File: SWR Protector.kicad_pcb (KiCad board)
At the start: 2 copper layers, 100 x 100 mm, 27 parts, among them J1 Barrel_Jack, J2 Barrel_Jack, J3 transceiver, J4 antenna, K2 ATX209, Q1 2N3904, T1 1:12, T2 1:12, U1 LM78L05_TO92, U2 LM358

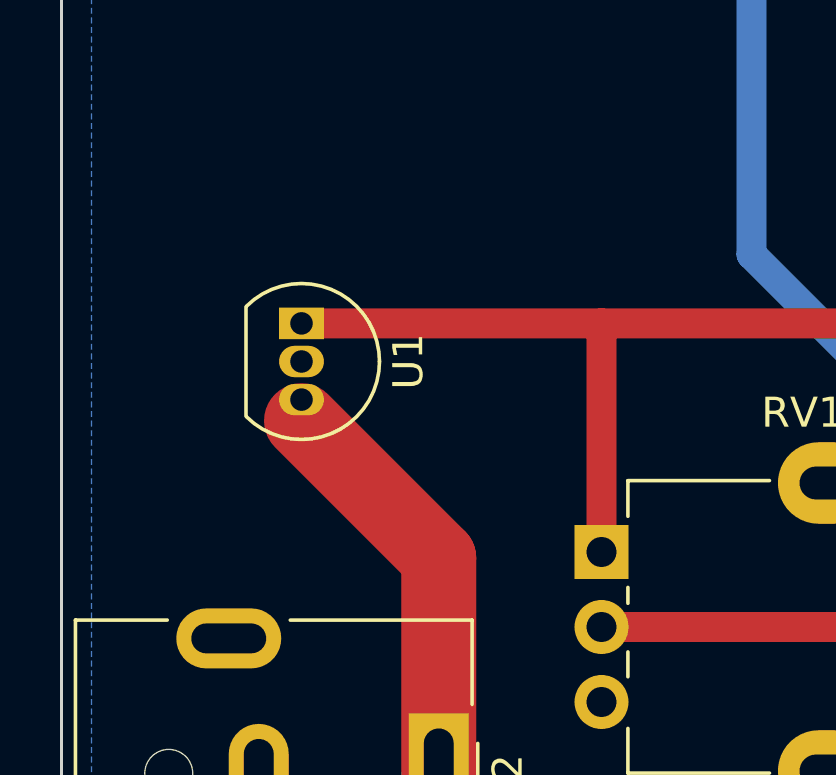
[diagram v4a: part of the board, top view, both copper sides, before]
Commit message: Added a couple of caps on the 5V regulator.
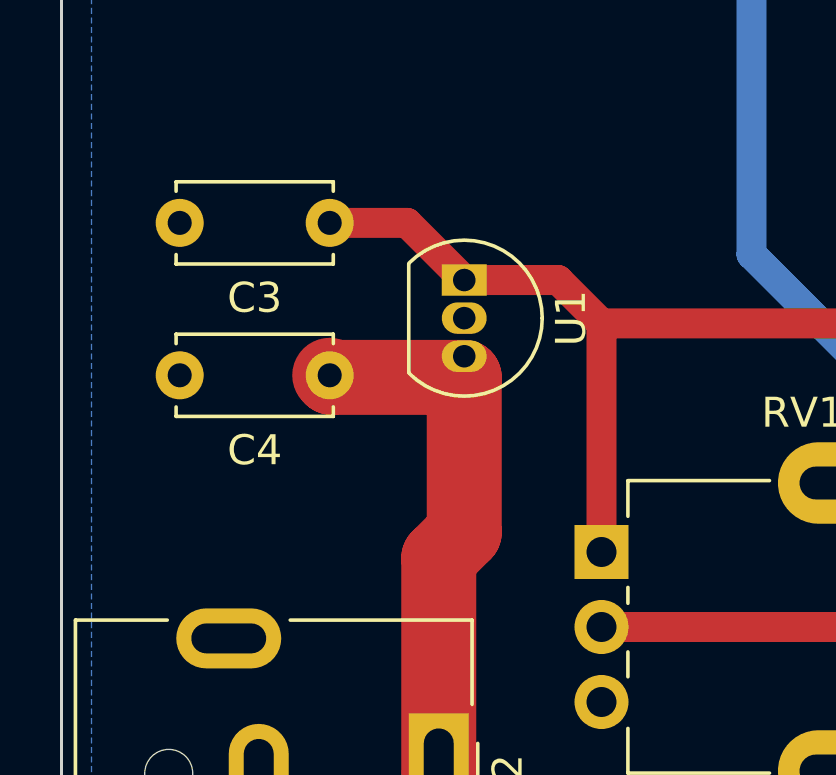
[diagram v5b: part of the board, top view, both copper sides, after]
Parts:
- added C3: 100 nF, Capacitor_THT:C_Disc_D5.0mm_W2.5mm_P5.00mm, F.Cu at (93.9, 120.7)
- added C4: 100 nF, Capacitor_THT:C_Disc_D5.0mm_W2.5mm_P5.00mm, F.Cu at (93.9, 125.7)
- moved U1 5.61 mm to (98.4, 122.6)
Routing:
- net +12V: track 82.4 -> 86.8 mm
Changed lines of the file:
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@@
   )
   (footprint "Package_TO_SOT_THT:TO-92_Inline" (layer "F.Cu")
-    (at 93 124 -90)
+    (at 98.425 122.555 -90)
     (descr "TO-92 leads in-line, narrow, oval pads, drill 0.75mm (see NXP sot054_po.pdf)")
     (tags "to-92 sc-43 sc-43a sot54 PA33 transistor")
@@
     )
   )
+  (footprint "Capacitor_THT:C_Disc_D5.0mm_W2.5mm_P5.00mm" (layer "F.Cu")
+    (at 93.94 120.65 180)
+    (descr "C, Disc series, Radial, pin pitch=5.00mm, , diameter*width=5*2.5mm^2, Capacitor, http://cdn-reichelt.de/documents/datenblatt/B300/DS_KERKO_TC.pdf")
+    (tags "C Disc series Radial pin pitch 5.00mm  diameter 5mm width 2.5mm Capacitor")
+    (property "Sheetfile" "SWR Protector.kicad_sch")
+    (property "Sheetname" "")
+    (property "ki_description" "Unpolarized capacitor")
+    (property "ki_keywords" "cap capacitor")
+    (attr through_hole)
+    (fp_text reference "C3" (at 2.5 -2.5) (layer "F.SilkS")
+        (effects (font (size 1 1) (thickness 0.15)))
+    )
+    (fp_text value "100 nF" (at 2.5 2.5) (layer "F.Fab")
+        (effects (font (size 1 1) (thickness 0.15)))
+    )
+    (fp_text user "${REFERENCE}" (at 2.5 0) (layer "F.Fab")
+        (effects (font (size 1 1) (thickness 0.15)))
+    )
+    (fp_line (start -0.12 -1.37) (end -0.12 -1.055)
+      (stroke (width 0.12) (type solid)) (layer "F.SilkS"))
+    (fp_line (start -0.12 -1.37) (end 5.12 -1.37)
+      (stroke (width 0.12) (type solid)) (layer "F.SilkS"))
+    (fp_line (start -0.12 1.055) (end -0.12 1.37)
+      (stroke (width 0.12) (type solid)) (layer "F.SilkS"))
+    (fp_line (start -0.12 1.37) (end 5.12 1.37)
+      (stroke (width 0.12) (type solid)) (layer "F.SilkS"))
+    (fp_line (start 5.12 -1.37) (end 5.12 -1.055)
+      (stroke (width 0.12) (type solid)) (layer "F.SilkS"))
+    (fp_line (start 5.12 1.055) (end 5.12 1.37)
+      (stroke (width 0.12) (type solid)) (layer "F.SilkS"))
+    (fp_line (start -1.05 -1.5) (end -1.05 1.5)
+      (stroke (width 0.05) (type solid)) (layer "F.CrtYd"))
+    (fp_line (start -1.05 1.5) (end 6.05 1.5)
+      (stroke (width 0.05) (type solid)) (layer "F.CrtYd"))
+    (fp_line (start 6.05 -1.5) (end -1.05 -1.5)
+      (stroke (width 0.05) (type solid)) (layer "F.CrtYd"))
+    (fp_line (start 6.05 1.5) (end 6.05 -1.5)
+      (stroke (width 0.05) (type solid)) (layer "F.CrtYd"))
+    (fp_line (start 0 -1.25) (end 0 1.25)
+      (stroke (width 0.1) (type solid)) (layer "F.Fab"))
+    (fp_line (start 0 1.25) (end 5 1.25)
+      (stroke (width 0.1) (type solid)) (layer "F.Fab"))
+    (fp_line (start 5 -1.25) (end 0 -1.25)
+      (stroke (width 0.1) (type solid)) (layer "F.Fab"))
+    (fp_line (start 5 1.25) (end 5 -1.25)
+      (stroke (width 0.1) (type solid)) (layer "F.Fab"))
+    (pad "1" thru_hole circle (at 0 0 180) (size 1.6 1.6) (drill 0.8) (layers "*.Cu" "*.Mask")
+      (net 4 "+5V") (pintype "passive"))
+    (pad "2" thru_hole circle (at 5 0 180) (size 1.6 1.6) (drill 0.8) (layers "*.Cu" "*.Mask")
+      (net 2 "GND") (pintype "passive"))
+    (model "${KICAD6_3DMODEL_DIR}/Capacitor_THT.3dshapes/C_Disc_D5.0mm_W2.5mm_P5.00mm.wrl"
+      (offset (xyz 0 0 0))
+      (scale (xyz 1 1 1))
+      (rotate (xyz 0 0 0))
+    )
+  )
   (footprint "Connector_BarrelJack:BarrelJack_CUI_PJ-063AH_Horizontal" (layer "F.Cu")
     (at 97.575 139 -90)
@@
     (pad "1" thru_hole rect (at 0 0) (size 4 4) (drill 2) (layers "*.Cu" "*.Mask")
       (net 3 "Net-(D4-K)") (pinfunction "1") (pintype "passive"))
+  )
+  (footprint "Capacitor_THT:C_Disc_D5.0mm_W2.5mm_P5.00mm" (layer "F.Cu")
+    (at 93.94 125.73 180)
+    (descr "C, Disc series, Radial, pin pitch=5.00mm, , diameter*width=5*2.5mm^2, Capacitor, http://cdn-reichelt.de/documents/datenblatt/B300/DS_KERKO_TC.pdf")
+    (tags "C Disc series Radial pin pitch 5.00mm  diameter 5mm width 2.5mm Capacitor")
+    (property "Sheetfile" "SWR Protector.kicad_sch")
+    (property "Sheetname" "")
+    (property "ki_description" "Unpolarized capacitor")
+    (property "ki_keywords" "cap capacitor")
+    (attr through_hole)
+    (fp_text reference "C4" (at 2.5 -2.5) (layer "F.SilkS")
+        (effects (font (size 1 1) (thickness 0.15)))
+    )
+    (fp_text value "100 nF" (at 2.5 2.5) (layer "F.Fab")
+        (effects (font (size 1 1) (thickness 0.15)))
+    )
+    (fp_text user "${REFERENCE}" (at 2.5 0) (layer "F.Fab")
+        (effects (font (size 1 1) (thickness 0.15)))
+    )
+    (fp_line (start -0.12 -1.37) (end -0.12 -1.055)
+      (stroke (width 0.12) (type solid)) (layer "F.SilkS"))
+    (fp_line (start -0.12 -1.37) (end 5.12 -1.37)
+      (stroke (width 0.12) (type solid)) (layer "F.SilkS"))
+    (fp_line (start -0.12 1.055) (end -0.12 1.37)
+      (stroke (width 0.12) (type solid)) (layer "F.SilkS"))
+    (fp_line (start -0.12 1.37) (end 5.12 1.37)
+      (stroke (width 0.12) (type solid)) (layer "F.SilkS"))
+    (fp_line (start 5.12 -1.37) (end 5.12 -1.055)
+      (stroke (width 0.12) (type solid)) (layer "F.SilkS"))
+    (fp_line (start 5.12 1.055) (end 5.12 1.37)
+      (stroke (width 0.12) (type solid)) (layer "F.SilkS"))
+    (fp_line (start -1.05 -1.5) (end -1.05 1.5)
+      (stroke (width 0.05) (type solid)) (layer "F.CrtYd"))
+    (fp_line (start -1.05 1.5) (end 6.05 1.5)
+      (stroke (width 0.05) (type solid)) (layer "F.CrtYd"))
+    (fp_line (start 6.05 -1.5) (end -1.05 -1.5)
+      (stroke (width 0.05) (type solid)) (layer "F.CrtYd"))
+    (fp_line (start 6.05 1.5) (end 6.05 -1.5)
+      (stroke (width 0.05) (type solid)) (layer "F.CrtYd"))
+    (fp_line (start 0 -1.25) (end 0 1.25)
+      (stroke (width 0.1) (type solid)) (layer "F.Fab"))
+    (fp_line (start 0 1.25) (end 5 1.25)
+      (stroke (width 0.1) (type solid)) (layer "F.Fab"))
+    (fp_line (start 5 -1.25) (end 0 -1.25)
+      (stroke (width 0.1) (type solid)) (layer "F.Fab"))
+    (fp_line (start 5 1.25) (end 5 -1.25)
+      (stroke (width 0.1) (type solid)) (layer "F.Fab"))
+    (pad "1" thru_hole circle (at 0 0 180) (size 1.6 1.6) (drill 0.8) (layers "*.Cu" "*.Mask")
+      (net 9 "+12V") (pintype "passive"))
+    (pad "2" thru_hole circle (at 5 0 180) (size 1.6 1.6) (drill 0.8) (layers "*.Cu" "*.Mask")
+      (net 2 "GND") (pintype "passive"))
+    (model "${KICAD6_3DMODEL_DIR}/Capacitor_THT.3dshapes/C_Disc_D5.0mm_W2.5mm_P5.00mm.wrl"
+      (offset (xyz 0 0 0))
+      (scale (xyz 1 1 1))
+      (rotate (xyz 0 0 0))
+    )
   )
   (footprint "Diode_THT:D_DO-41_SOD81_P10.16mm_Horizontal" (layer "F.Cu")
@@
   (segment (start 165.08 112) (end 165.08 117.92) (width 1) (layer "F.Cu") (net 4))
   (segment (start 165.08 103.08) (end 165 103) (width 1) (layer "F.Cu") (net 4))
-  (segment (start 93 124) (end 103 124) (width 1) (layer "F.Cu") (net 4))
+  (segment (start 101.555 122.555) (end 103 124) (width 1) (layer "F.Cu") (net 4))
   (segment (start 159 124) (end 134 124) (width 1) (layer "F.Cu") (net 4))
   (segment (start 129 124) (end 103 124) (width 1) (layer "F.Cu") (net 4))
   (segment (start 165.08 112) (end 165.08 103.08) (width 1) (layer "F.Cu") (net 4))
+  (segment (start 93.94 120.65) (end 96.52 120.65) (width 1) (layer "F.Cu") (net 4))
   (segment (start 134 124) (end 129 124) (width 1) (layer "F.Cu") (net 4))
+  (segment (start 96.52 120.65) (end 98.425 122.555) (width 1) (layer "F.Cu") (net 4))
   (segment (start 165.08 117.92) (end 159 124) (width 1) (layer "F.Cu") (net 4))
   (segment (start 134 130.62) (end 134 124) (width 1) (layer "F.Cu") (net 4))
@@
   (segment (start 103 124) (end 103 131.62) (width 1) (layer "F.Cu") (net 4))
   (segment (start 129 130) (end 129 124) (width 1) (layer "F.Cu") (net 4))
+  (segment (start 98.425 122.555) (end 101.555 122.555) (width 1) (layer "F.Cu") (net 4))
   (segment (start 147 103) (end 147 108.84) (width 1) (layer "F.Cu") (net 5))
   (segment (start 150.16 112) (end 142.54 119.62) (width 1) (layer "F.Cu") (net 5))
@@
   (segment (start 165.71 65.38) (end 165.735 65.405) (width 1) (layer "F.Cu") (net 8))
   (segment (start 166 77.84) (end 166 73) (width 1) (layer "F.Cu") (net 8))
+  (segment (start 93.94 125.73) (end 94.01 125.8) (width 2.5) (layer "F.Cu") (net 9))
+  (segment (start 98.425 130.97) (end 97.575 131.82) (width 2.5) (layer "F.Cu") (net 9))
+  (segment (start 98.425 125.8) (end 98.425 130.97) (width 2.5) (layer "F.Cu") (net 9))
   (segment (start 97.575 139) (end 97.575 131.82) (width 2.5) (layer "F.Cu") (net 9))
-  (segment (start 97.575 131.82) (end 93 127.245) (width 2.5) (layer "F.Cu") (net 9))
+  (segment (start 94.01 125.8) (end 98.425 125.8) (width 2.5) (layer "F.Cu") (net 9))
   (segment (start 150.38 138.62) (end 145 144) (width 2.5) (layer "B.Cu") (net 9))
   (segment (start 159 138.62) (end 150.38 138.62) (width 2.5) (layer "B.Cu") (net 9))
